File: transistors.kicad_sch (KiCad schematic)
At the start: 18 parts, among them J11 Transistor_2, J12 Transistor_1, J13 Transistor_4, J14 Transistor_.3, Q1 DMN2011UTS, Q2 DMN2011UTS, Q3 DMN2011UTS, Q4 DMN2011UTS

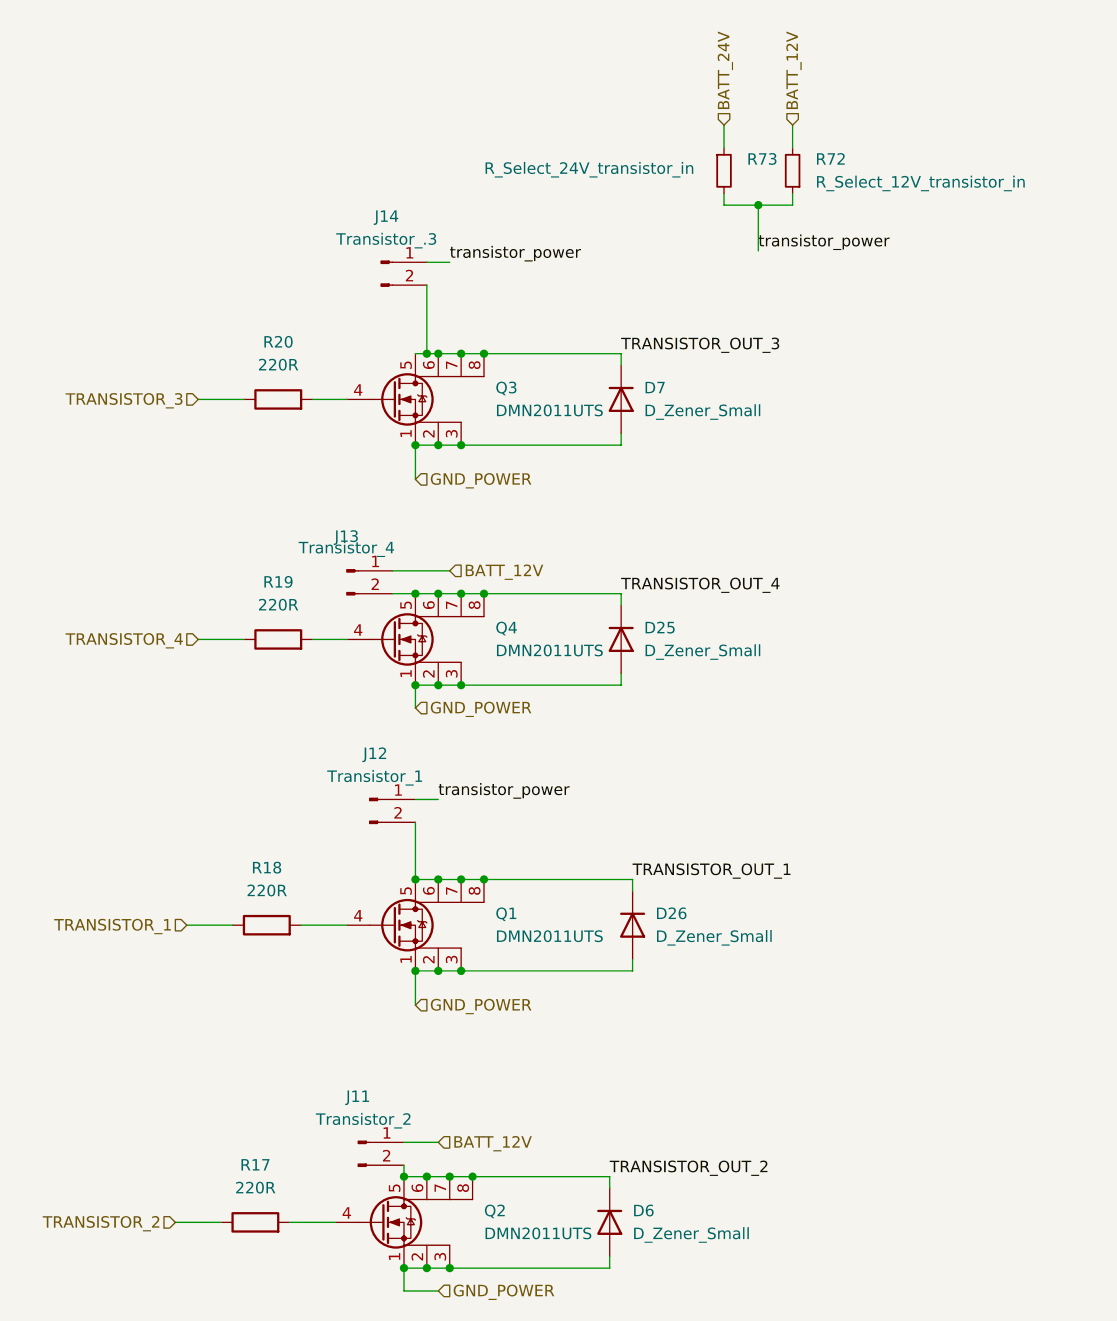
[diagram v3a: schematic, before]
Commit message: update BOM + add big capas (do not take DNP into account)
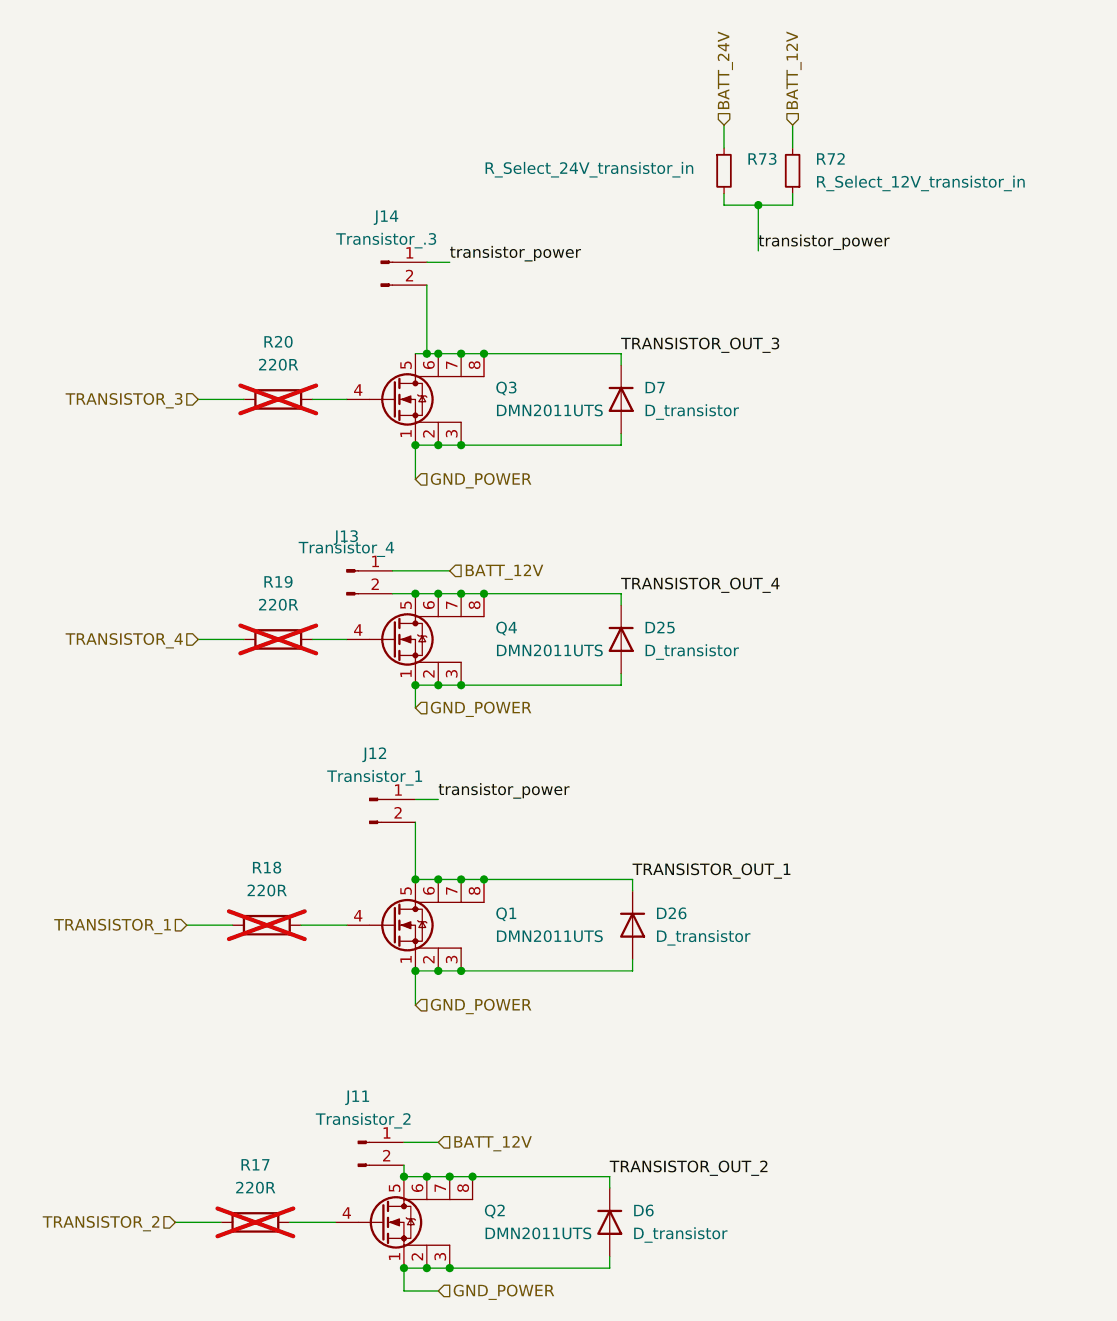
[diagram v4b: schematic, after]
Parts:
- D25, D26, D6, D7: value D_Zener_Small -> D_transistor
- R17, R18, R19, R20: now not fitted
- R72, R73: LCSC# (none) -> C2907406
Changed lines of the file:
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@@
 		)
 		(instances
+			(project "transistors"
+				(path "/dd7715f7-4665-4e2d-be0e-5eaf3bd7a739"
+					(reference "J?")
+					(unit 1)
+				)
+			)
 			(project ""
 				(path "/e63e39d7-6ac0-4ffd-8aa3-1841a4541b55/8cf8b4bb-2251-4ebd-baba-4f57c988e66e"
@@
 			)
 		)
-		(property "Value" "D_Zener_Small"
+		(property "Value" "D_transistor"
 			(at 215.9 115.5699 90)
 			(effects
@@
 		)
 		(instances
+			(project "transistors"
+				(path "/dd7715f7-4665-4e2d-be0e-5eaf3bd7a739"
+					(reference "D?")
+					(unit 1)
+				)
+			)
 			(project ""
 				(path "/e63e39d7-6ac0-4ffd-8aa3-1841a4541b55/8cf8b4bb-2251-4ebd-baba-4f57c988e66e"
@@
 		)
 		(instances
+			(project "transistors"
+				(path "/dd7715f7-4665-4e2d-be0e-5eaf3bd7a739"
+					(reference "Q?")
+					(unit 1)
+				)
+			)
 			(project ""
 				(path "/e63e39d7-6ac0-4ffd-8aa3-1841a4541b55/8cf8b4bb-2251-4ebd-baba-4f57c988e66e"
@@
 			)
 		)
-		(property "Value" "D_Zener_Small"
+		(property "Value" "D_transistor"
 			(at 213.36 148.5899 90)
 			(effects
@@
 		)
 		(instances
+			(project "transistors"
+				(path "/dd7715f7-4665-4e2d-be0e-5eaf3bd7a739"
+					(reference "D?")
+					(unit 1)
+				)
+			)
 			(project ""
 				(path "/e63e39d7-6ac0-4ffd-8aa3-1841a4541b55/8cf8b4bb-2251-4ebd-baba-4f57c988e66e"
@@
 		(in_bom yes)
 		(on_board yes)
-		(dnp no)
+		(dnp yes)
 		(fields_autoplaced yes)
 		(property "Reference" "R17"
@@
 		)
 		(instances
+			(project "transistors"
+				(path "/dd7715f7-4665-4e2d-be0e-5eaf3bd7a739"
+					(reference "R?")
+					(unit 1)
+				)
+			)
 			(project ""
 				(path "/e63e39d7-6ac0-4ffd-8aa3-1841a4541b55/8cf8b4bb-2251-4ebd-baba-4f57c988e66e"
@@
 			)
 		)
-		(property "Value" "D_Zener_Small"
+		(property "Value" "D_transistor"
 			(at 214.63 83.8199 90)
 			(effects
@@
 		)
 		(instances
+			(project "transistors"
+				(path "/dd7715f7-4665-4e2d-be0e-5eaf3bd7a739"
+					(reference "D?")
+					(unit 1)
+				)
+			)
 			(project ""
 				(path "/e63e39d7-6ac0-4ffd-8aa3-1841a4541b55/8cf8b4bb-2251-4ebd-baba-4f57c988e66e"
@@
 		(in_bom yes)
 		(on_board yes)
-		(dnp no)
+		(dnp yes)
 		(fields_autoplaced yes)
 		(property "Reference" "R19"
@@
 		)
 		(instances
+			(project "transistors"
+				(path "/dd7715f7-4665-4e2d-be0e-5eaf3bd7a739"
+					(reference "R?")
+					(unit 1)
+				)
+			)
 			(project ""
 				(path "/e63e39d7-6ac0-4ffd-8aa3-1841a4541b55/8cf8b4bb-2251-4ebd-baba-4f57c988e66e"
@@
 		)
 		(instances
+			(project "transistors"
+				(path "/dd7715f7-4665-4e2d-be0e-5eaf3bd7a739"
+					(reference "J?")
+					(unit 1)
+				)
+			)
 			(project ""
 				(path "/e63e39d7-6ac0-4ffd-8aa3-1841a4541b55/8cf8b4bb-2251-4ebd-baba-4f57c988e66e"
@@
 		)
 		(instances
+			(project "transistors"
+				(path "/dd7715f7-4665-4e2d-be0e-5eaf3bd7a739"
+					(reference "J?")
+					(unit 1)
+				)
+			)
 			(project ""
 				(path "/e63e39d7-6ac0-4ffd-8aa3-1841a4541b55/8cf8b4bb-2251-4ebd-baba-4f57c988e66e"
@@
 			)
 		)
-		(pin "2"
-		)
-		(pin "1"
-		)
-		(instances
+		(property "LCSC#" "C2907406"
+			(at 223.52 30.48 0)
+			(effects
+				(font
+					(size 1.27 1.27)
+				)
+				(hide yes)
+			)
+		)
+		(pin "2"
+		)
+		(pin "1"
+		)
+		(instances
+			(project "transistors"
+				(path "/dd7715f7-4665-4e2d-be0e-5eaf3bd7a739"
+					(reference "R?")
+					(unit 1)
+				)
+			)
 			(project "carte_servo"
 				(path "/e63e39d7-6ac0-4ffd-8aa3-1841a4541b55/8cf8b4bb-2251-4ebd-baba-4f57c988e66e"
@@
 			)
 		)
-		(property "Value" "D_Zener_Small"
+		(property "Value" "D_transistor"
 			(at 214.63 57.1499 90)
 			(effects
@@
 		)
 		(instances
+			(project "transistors"
+				(path "/dd7715f7-4665-4e2d-be0e-5eaf3bd7a739"
+					(reference "D?")
+					(unit 1)
+				)
+			)
 			(project ""
 				(path "/e63e39d7-6ac0-4ffd-8aa3-1841a4541b55/8cf8b4bb-2251-4ebd-baba-4f57c988e66e"
@@
 		(in_bom yes)
 		(on_board yes)
-		(dnp no)
+		(dnp yes)
 		(fields_autoplaced yes)
 		(property "Reference" "R20"
@@
 		)
 		(instances
+			(project "transistors"
+				(path "/dd7715f7-4665-4e2d-be0e-5eaf3bd7a739"
+					(reference "R?")
+					(unit 1)
+				)
+			)
 			(project ""
 				(path "/e63e39d7-6ac0-4ffd-8aa3-1841a4541b55/8cf8b4bb-2251-4ebd-baba-4f57c988e66e"
@@
 		)
 		(instances
+			(project "transistors"
+				(path "/dd7715f7-4665-4e2d-be0e-5eaf3bd7a739"
+					(reference "Q?")
+					(unit 1)
+				)
+			)
 			(project ""
 				(path "/e63e39d7-6ac0-4ffd-8aa3-1841a4541b55/8cf8b4bb-2251-4ebd-baba-4f57c988e66e"
@@
 			)
 		)
-		(pin "2"
-		)
-		(pin "1"
-		)
-		(instances
+		(property "LCSC#" "C2907406"
+			(at 231.14 30.48 0)
+			(effects
+				(font
+					(size 1.27 1.27)
+				)
+				(hide yes)
+			)
+		)
+		(pin "2"
+		)
+		(pin "1"
+		)
+		(instances
+			(project "transistors"
+				(path "/dd7715f7-4665-4e2d-be0e-5eaf3bd7a739"
+					(reference "R?")
+					(unit 1)
+				)
+			)
 			(project "carte_servo"
 				(path "/e63e39d7-6ac0-4ffd-8aa3-1841a4541b55/8cf8b4bb-2251-4ebd-baba-4f57c988e66e"
@@
 		)
 		(instances
+			(project "transistors"
+				(path "/dd7715f7-4665-4e2d-be0e-5eaf3bd7a739"
+					(reference "Q?")
+					(unit 1)
+				)
+			)
 			(project ""
 				(path "/e63e39d7-6ac0-4ffd-8aa3-1841a4541b55/8cf8b4bb-2251-4ebd-baba-4f57c988e66e"
@@
 		)
 		(instances
+			(project "transistors"
+				(path "/dd7715f7-4665-4e2d-be0e-5eaf3bd7a739"
+					(reference "Q?")
+					(unit 1)
+				)
+			)
 			(project ""
 				(path "/e63e39d7-6ac0-4ffd-8aa3-1841a4541b55/8cf8b4bb-2251-4ebd-baba-4f57c988e66e"
@@
 		)
 		(instances
+			(project "transistors"
+				(path "/dd7715f7-4665-4e2d-be0e-5eaf3bd7a739"
+					(reference "J?")
+					(unit 1)
+				)
+			)
 			(project ""
 				(path "/e63e39d7-6ac0-4ffd-8aa3-1841a4541b55/8cf8b4bb-2251-4ebd-baba-4f57c988e66e"
@@
 		(in_bom yes)
 		(on_board yes)
-		(dnp no)
+		(dnp yes)
 		(fields_autoplaced yes)
 		(property "Reference" "R18"
@@
 		)
 		(instances
+			(project "transistors"
+				(path "/dd7715f7-4665-4e2d-be0e-5eaf3bd7a739"
+					(reference "R?")
+					(unit 1)
+				)
+			)
 			(project ""
 				(path "/e63e39d7-6ac0-4ffd-8aa3-1841a4541b55/8cf8b4bb-2251-4ebd-baba-4f57c988e66e"
@@
 		)
 	)
+	(sheet_instances
+		(path "/"
+			(page "1")
+		)
+	)
+	(embedded_fonts no)
 )

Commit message: fix DNP (was just for checking what was to be bought)
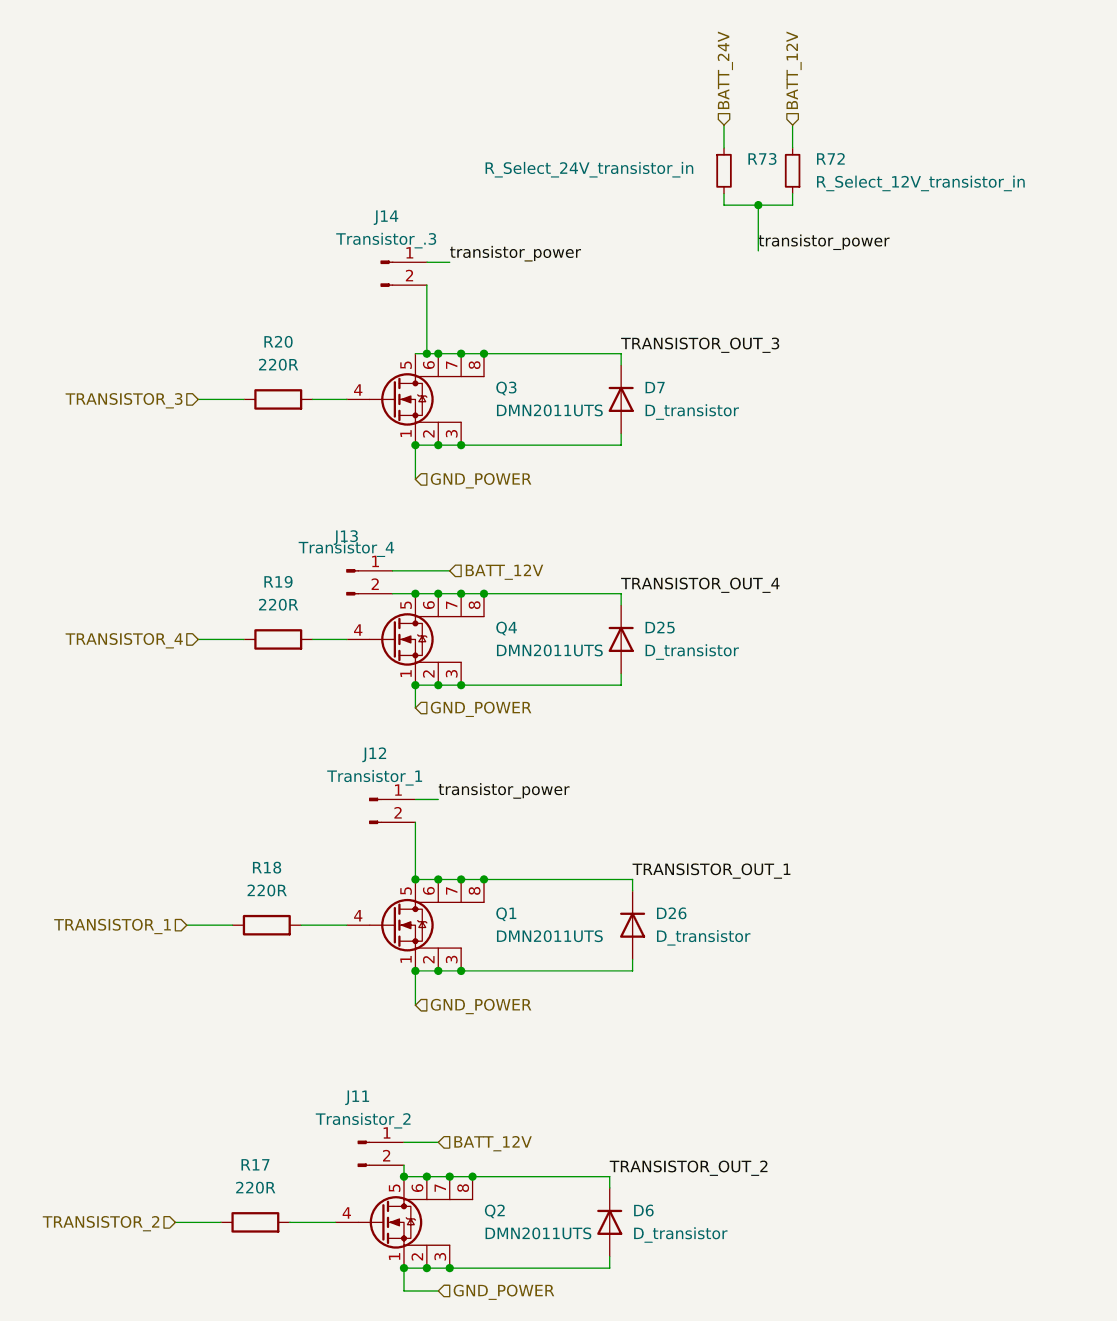
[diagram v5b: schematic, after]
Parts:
- R17, R18, R19, R20: now fitted
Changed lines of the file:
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@@
 		(in_bom yes)
 		(on_board yes)
-		(dnp yes)
+		(dnp no)
 		(fields_autoplaced yes)
 		(property "Reference" "R17"
@@
 		(in_bom yes)
 		(on_board yes)
-		(dnp yes)
+		(dnp no)
 		(fields_autoplaced yes)
 		(property "Reference" "R19"
@@
 		(in_bom yes)
 		(on_board yes)
-		(dnp yes)
+		(dnp no)
 		(fields_autoplaced yes)
 		(property "Reference" "R20"
@@
 		(in_bom yes)
 		(on_board yes)
-		(dnp yes)
+		(dnp no)
 		(fields_autoplaced yes)
 		(property "Reference" "R18"

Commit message: update to Kicad 10 + start fixing warnings
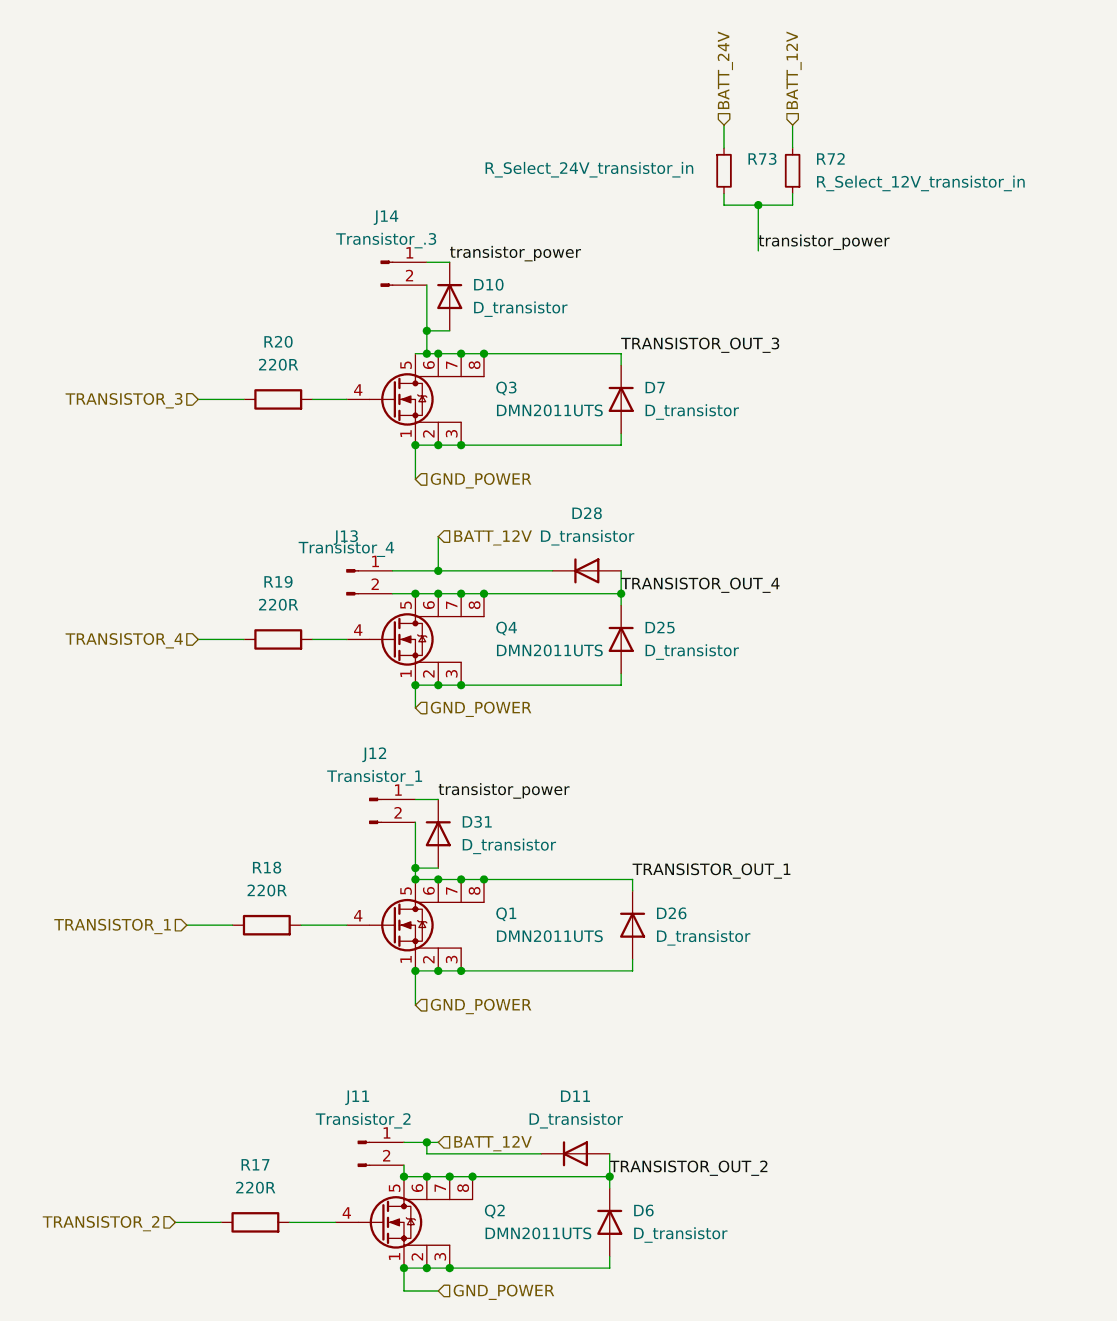
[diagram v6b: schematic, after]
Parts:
- added D10, D11, D28, D31: D_transistor, Diode_SMD:D_SOD-123, symbol Device:D
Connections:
- net BATT_12V: now also D11.1 (K), D28.1 (K)
- net TRANSISTOR_OUT_1: now also D31.2 (A)
- net TRANSISTOR_OUT_2: now also D11.2 (A)
- net TRANSISTOR_OUT_3: now also D10.2 (A)
- net TRANSISTOR_OUT_4: now also D28.2 (A)
- net transistor_power: now also D10.1 (K), D31.1 (K)
